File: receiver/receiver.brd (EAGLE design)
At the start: 100 x 80 mm, 3 parts, among them Q1 3.3

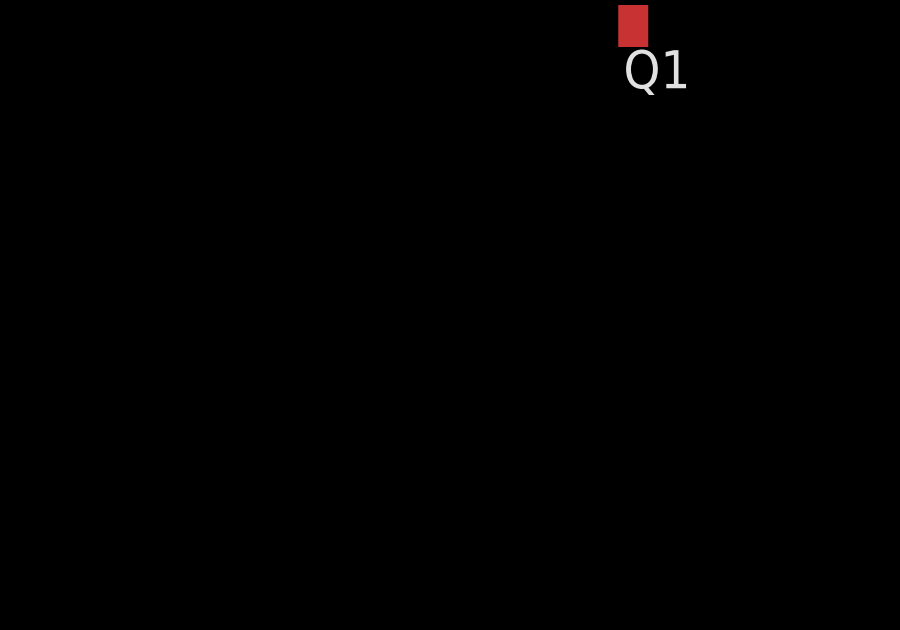
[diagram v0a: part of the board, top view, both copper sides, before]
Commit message: add yc164 resistor to receiver
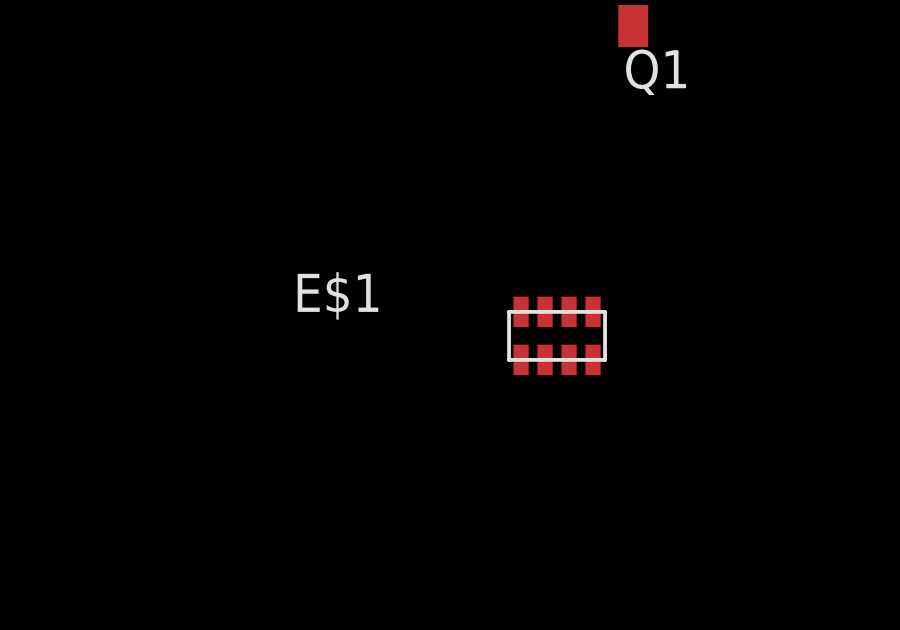
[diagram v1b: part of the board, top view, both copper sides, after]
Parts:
- added E$1: (no value), yc164:YC164
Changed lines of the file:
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@@
 <element name="U$1" library="cree_plcc4_rgb_led" package="4-PLCC" value="" x="45.72" y="25.4"/>
 <element name="Q1" library="adafruit" package="SOT23" value="3.3" x="49.53" y="53.34" rot="R180"/>
+<element name="E$1" library="yc164" package="YC164" value="" x="46.99" y="41.91"/>
 </elements>
 <signals>

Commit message: layout components
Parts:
- added U$2: CORE51822B, core51822b:CORE51822B
- added U$3: YC164, yc164:YC164
- E$1: value (none) -> YC164
- U$1: value (none) -> CREE_PLCC4_RGB_LED
- moved U$1 44.7 mm to (34.3, 68.6)
- moved E$1 25.4 mm to (31.8, 62.2)
- moved B1 23.9 mm to (38.1, 41.9)
- moved Q1 15.5 mm to (36.8, 62.2), turned to 0 degrees
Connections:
- removed net RAW: B1.24
- new net N$1: B1.24, Q1.3, U$1.P$2
- new net N$10: U$1.P$4, U$3.P$6
- new net N$11: U$1.P$1, U$3.P$5
- new net N$12: U$3.P$2, U$3.P$3
- new net N$14: U$1.P$3, U$3.P$8
- new net N$2: B1.22
- new net N$3: B1.20, U$3.P$4
- new net N$4: B1.19, U$3.P$1
- new net N$5: B1.5, U$3.P$7
- new net N$6: B1.6
- new net N$7: B1.1, E$1.P$7, E$1.P$8
- new net N$8: E$1.P$1, E$1.P$2, E$1.P$3, E$1.P$4, U$2.P25
- net GND: now also E$1.P$5, Q1.1, U$2.GND0, U$2.GND1
- net VCC: now also Q1.2, U$2.VCC
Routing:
- net GND: track 0.00 -> 78.5 mm, vias 0 -> 1
- net N$5: track 0.00 -> 56.8 mm, vias 0 -> 1
- net N$11: track 0.00 -> 43.5 mm
- net N$14: track 0.00 -> 34.3 mm, vias 0 -> 2
- net N$10: track 0.00 -> 33.5 mm
- net VCC: track 0.00 -> 20.9 mm
- net N$1: track 0.00 -> 15.3 mm, vias 0 -> 2
- net N$7: track 0.00 -> 0.81 mm
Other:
- board size 100 x 80 mm -> 47.9 x 59.7 mm

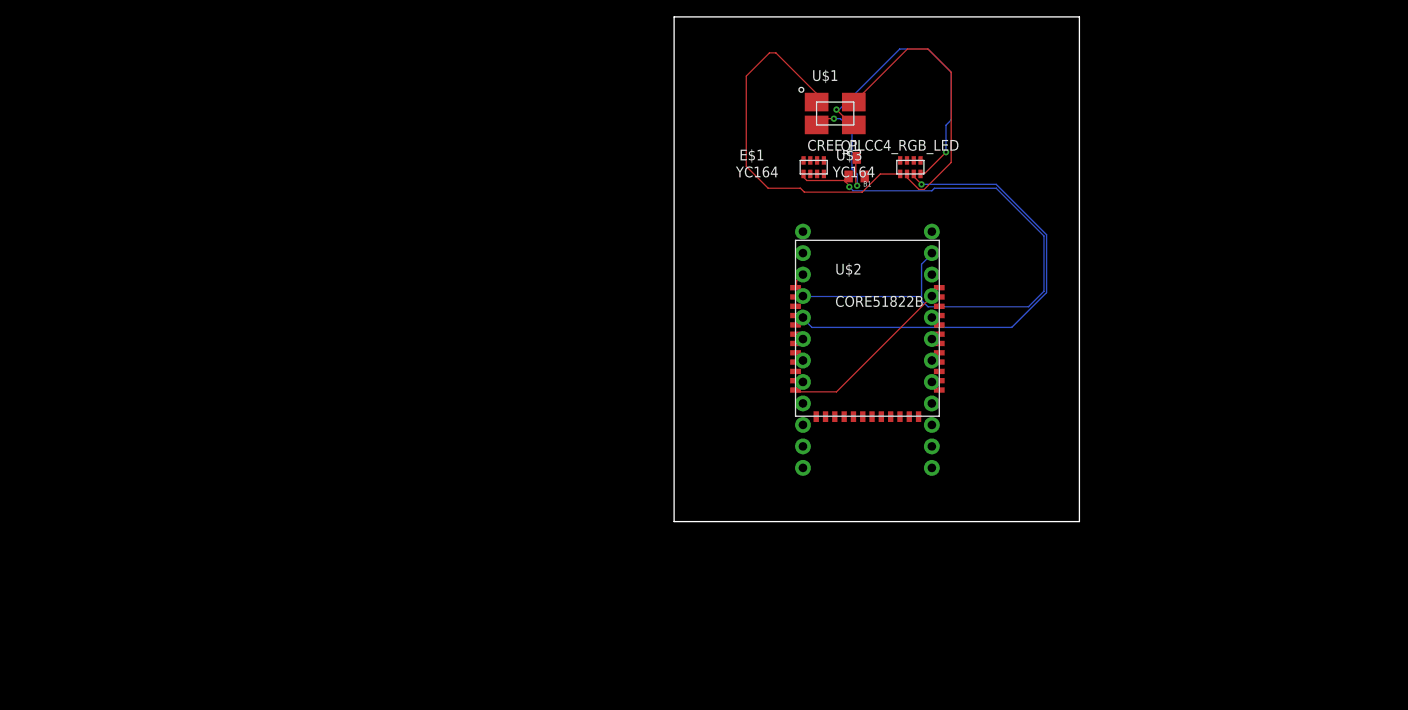
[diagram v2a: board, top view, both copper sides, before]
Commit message: add pts525-sm15 spst push button switch
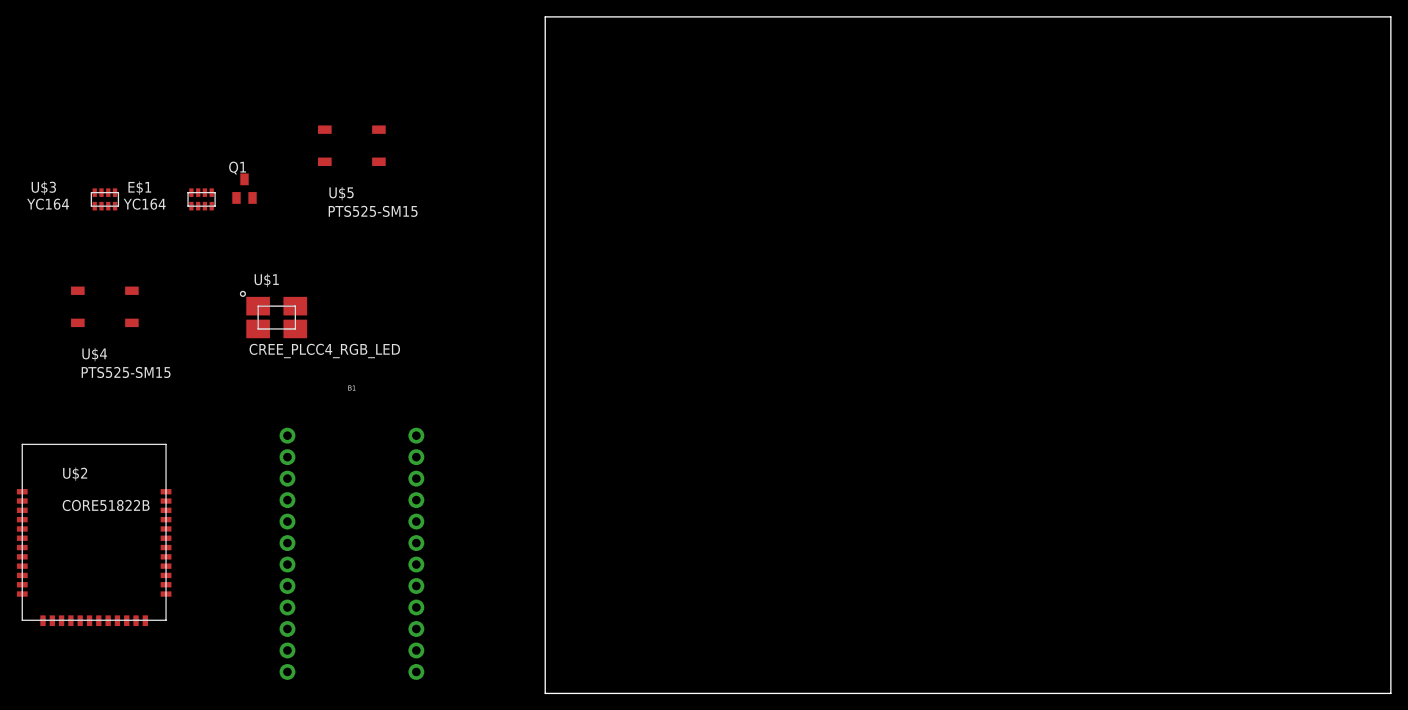
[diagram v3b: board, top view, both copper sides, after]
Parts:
- added U$4, U$5: PTS525-SM15, pts525-sm15:PTS525-SM15
- moved U$3 95.3 mm to (-52.1, 58.4)
- moved U$2 94.6 mm to (-53.3, 19.1)
- moved E$1 72.5 mm to (-40.6, 58.4)
- moved Q1 72.4 mm to (-35.6, 59.7)
- moved U$1 70.3 mm to (-31.8, 44.5)
- moved B1 65.6 mm to (-22.9, 17.8)
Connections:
- net N$1 renamed VIN
- net N$3 renamed LED-B
- net N$4 renamed LED-R
- net N$5 renamed LED-G
- net N$7 renamed TXO
- net N$8 renamed TXO-DIV
- removed net N$2: B1.22
- removed net N$6: B1.6
- new net PAIR: B1.6, U$4.P$3, U$4.P$4
- new net RESET: B1.22, U$5.P$3, U$5.P$4
- net GND: now also U$4.P$1, U$4.P$2, U$5.P$1, U$5.P$2
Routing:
- net GND: track 78.5 -> 0.00 mm, vias 1 -> 0
- net LED-G: track 56.8 -> 0.00 mm, vias 1 -> 0
- net N$11: track 43.5 -> 0.00 mm
- net N$14: track 34.3 -> 0.00 mm, vias 2 -> 0
- net N$10: track 33.5 -> 0.00 mm
- net VCC: track 20.9 -> 0.00 mm
- net VIN: track 15.3 -> 0.00 mm, vias 2 -> 0
- net TXO: track 0.81 -> 0.00 mm
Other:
- board size 47.9 x 59.7 mm -> 100 x 80 mm

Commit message: update board
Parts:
- removed B1: SPARKFUN_PRO_MICRO, SparkFun-Boards:SPARKFUN_PRO_MICRO
- added U$6, U$7: PROMICRO_HEADER, promicro_header:PROMICRO_HEADER
- moved U$2 134.7 mm to (78.7, 45.7)
- moved E$1 98.6 mm to (57.1, 45.7)
- moved Q1 94.0 mm to (55.9, 38.1)
- moved U$3 90.9 mm to (38.1, 47.0)
- moved U$4 86.2 mm to (31.8, 25.4)
- moved U$1 66.2 mm to (34.3, 39.4)
- moved U$5 52.2 mm to (11.4, 25.4)
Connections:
- new net ???: U$2.SWCLK
- new net ????: U$2.SWDIO
- new net ????????: U$6.P$4
- new net RXI: U$2.P24, U$7.P$2
- net GND: now also U$6.P$2, U$7.P$3, U$7.P$4; no longer B1.23, B1.3, B1.4
- net LED-B: now also U$6.P$5; no longer B1.20
- net LED-G: now also U$7.P$5; no longer B1.5
- net LED-R: now also U$6.P$6; no longer B1.19
- net PAIR: now also U$2.P29, U$7.P$6; no longer B1.6
- net RESET: now also U$6.P$3; no longer B1.22
- net TXO: now also U$7.P$1; no longer B1.1
- net VCC: no longer B1.21
- net VIN: now also U$6.P$1; no longer B1.24
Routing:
- net RESET: track 0.00 -> 67.5 mm
- net PAIR: track 0.00 -> 54.5 mm
- net VIN: track 0.00 -> 52.8 mm
- net VCC: track 0.00 -> 47.8 mm
- net LED-B: track 0.00 -> 18.1 mm
- net LED-R: track 0.00 -> 18.1 mm
- net TXO-DIV: track 0.00 -> 15.8 mm
- net N$14: track 0.00 -> 10.1 mm
- net N$11: track 0.00 -> 10.1 mm
- net N$10: track 0.00 -> 6.02 mm
- net N$12: track 0.00 -> 0.98 mm
- net TXO: track 0.00 -> 0.90 mm
- added copper zone on layer 1, net GND

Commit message: re-route
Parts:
- removed E$1, U$3: YC164, yc164:YC164
- removed Q1: 3.3, adafruit:SOT23
- removed U$1: CREE_PLCC4_RGB_LED, cree_plcc4_rgb_led:4-PLCC
- removed U$2: CORE51822B, core51822b:CORE51822B
- removed U$4, U$5: PTS525-SM15, pts525-sm15:PTS525-SM15
- removed U$6, U$7: PROMICRO_HEADER, promicro_header:PROMICRO_HEADER
- added B1, B2: PTS525-SM15, pts525-sm15:PTS525-SM15
- added D1: CREE_PLCC4_RGB_LED, cree_plcc4_rgb_led:4-PLCC
- added P1, P2: PROMICRO_HEADER, promicro_header:PROMICRO_HEADER
- added RA1, RA2: YC164, yc164:YC164
- added U1: CORE51822B, core51822b:CORE51822B
- added U2: 3.3, adafruit:SOT23
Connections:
- removed net ????????: U$6.P$4
- net ???: now also U1.SWCLK; no longer U$2.SWCLK
- net ????: now also U1.SWDIO; no longer U$2.SWDIO
- net GND: now also B1.P$1, B1.P$2, B2.P$1, B2.P$2, P1.P$3, P1.P$4, P2.P$2, RA2.P$5, U1.GND0, U1.GND1, U2.1; no longer E$1.P$5, Q1.1, U$2.GND0, U$2.GND1, U$4.P$1, U$4.P$2, U$5.P$1, U$5.P$2, U$6.P$2, U$7.P$3, U$7.P$4
- net LED-B: now also P2.P$5, RA1.P$4; no longer U$3.P$4, U$6.P$5
- net LED-G: now also P1.P$5, RA1.P$7; no longer U$3.P$7, U$7.P$5
- net LED-R: now also P2.P$6, RA1.P$1; no longer U$3.P$1, U$6.P$6
- net N$10: now also D1.P$4, RA1.P$6; no longer U$1.P$4, U$3.P$6
- net N$11: now also D1.P$1, RA1.P$5; no longer U$1.P$1, U$3.P$5
- net N$12: now also RA1.P$2, RA1.P$3; no longer U$3.P$2, U$3.P$3
- net N$14: now also D1.P$3, RA1.P$8; no longer U$1.P$3, U$3.P$8
- net PAIR: now also B1.P$3, B1.P$4, P1.P$6, U1.P29; no longer U$2.P29, U$4.P$3, U$4.P$4, U$7.P$6
- net RESET: now also B2.P$3, B2.P$4, P2.P$3; no longer U$5.P$3, U$5.P$4, U$6.P$3
- net RXI: now also P1.P$2, U1.P24; no longer U$2.P24, U$7.P$2
- net TXO: now also P1.P$1, RA2.P$7, RA2.P$8; no longer E$1.P$7, E$1.P$8, U$7.P$1
- net TXO-DIV: now also RA2.P$1, RA2.P$2, RA2.P$3, RA2.P$4, U1.P25; no longer E$1.P$1, E$1.P$2, E$1.P$3, E$1.P$4, U$2.P25
- net VCC: now also U1.VCC, U2.2; no longer Q1.2, U$2.VCC
- net VIN: now also D1.P$2, P2.P$1, U2.3; no longer Q1.3, U$1.P$2, U$6.P$1
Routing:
- net VCC: track 47.8 -> 9.23 mm
- net RESET: track 67.5 -> 31.1 mm
- net PAIR: track 54.5 -> 18.9 mm
- net RXI: track 0.00 -> 29.2 mm
- net VIN: track 52.8 -> 30.4 mm
- net LED-B: track 18.1 -> 6.63 mm
- net LED-R: track 18.1 -> 10.8 mm
- net N$11: track 10.1 -> 4.47 mm
- net N$14: track 10.1 -> 12.1 mm
- net N$10: track 6.02 -> 7.64 mm

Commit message: update board
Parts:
- U2: value 3.3 -> AZ1117IH; device adafruit:SOT23 -> az1117ih:AZ1117IH
- moved U2 3.06 mm to (56.1, 55.7)
- moved RA1 2.80 mm to (49.0, 57.8)
- moved RA2 2.80 mm to (49.0, 54.2)
- moved D1 1.30 mm to (44.3, 56.4)
- moved U1 1.02 mm to (72.1, 56.1)
- moved B1 0.13 mm to (55.9, 49.7)
- moved B2 0.13 mm to (47.1, 49.7), turned to 180 degrees
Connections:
- net GND: now also U2.ADJ/GND; no longer U2.1
- net VCC: now also U2.OUTPUT, U2.VOUT; no longer U2.2
- net VIN: now also U2.INPUT; no longer U2.3
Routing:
- net PAIR: track 18.9 -> 70.0 mm
- net VIN: track 30.4 -> 55.4 mm
- net RESET: track 31.1 -> 52.1 mm
- net TXO-DIV: track 15.4 -> 33.1 mm
- net LED-B: track 6.63 -> 15.6 mm
- net TXO: track 0.92 -> 9.30 mm
- net VCC: track 9.23 -> 16.8 mm
- net LED-R: track 10.8 -> 18.2 mm
- net N$14: track 12.1 -> 8.75 mm
- net N$10: track 7.64 -> 5.83 mm
- net RXI: track 29.2 -> 30.1 mm
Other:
- board text added: "Jesse Martin"
- board text added: "Kbd Receiver Version 1"

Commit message: include programming header on board
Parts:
- added U$1: PROG_HEADER, prog_header:PROG_HEADER
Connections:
- removed net ???: U1.SWCLK
- removed net ????: U1.SWDIO
- new net SWCLK: U$1.SWCLK, U1.SWCLK
- new net SWDIO: U$1.SWDIO, U1.SWDIO
- net GND: now also U$1.GND
- net VCC: now also U$1.VCC
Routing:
- net VCC: track 16.8 -> 54.8 mm
- net SWCLK: track 0.00 -> 4.75 mm
- net SWDIO: track 0.00 -> 3.33 mm
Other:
- board size 100 x 80 mm -> 49.2 x 26.7 mm
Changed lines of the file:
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@@
 <setting verticaltext="up"/>
 </settings>
-<grid distance="15.25" unitdist="mm" unit="mm" style="lines" multiple="1" display="yes" altdistance="5" altunitdist="mil" altunit="mil"/>
+<grid distance="2.54" unitdist="mm" unit="mm" style="lines" multiple="1" display="yes" altdistance="5" altunitdist="mil" altunit="mil"/>
 <layers>
 <layer number="1" name="Top" color="4" fill="1" visible="yes" active="yes"/>
@@
 <board>
 <plain>
-<wire x1="0" y1="0" x2="100" y2="0" width="0" layer="20"/>
-<wire x1="100" y1="0" x2="100" y2="80" width="0" layer="20"/>
-<wire x1="100" y1="80" x2="0" y2="80" width="0" layer="20"/>
-<wire x1="0" y1="80" x2="0" y2="0" width="0" layer="20"/>
+<wire x1="38.1" y1="40.64" x2="87.3" y2="40.64" width="0" layer="20"/>
+<wire x1="87.3" y1="40.64" x2="87.3" y2="67.3" width="0" layer="20"/>
+<wire x1="87.3" y1="67.3" x2="38.1" y2="67.3" width="0" layer="20"/>
+<wire x1="38.1" y1="67.3" x2="38.1" y2="40.64" width="0" layer="20"/>
 <text x="65.074" y="63.667" size="1.778" layer="25" font="vector">Jesse Martin</text>
 <text x="67.487" y="54.777" size="1.27" layer="25" font="vector">Kbd Receiver
@@
 <element name="P1" library="promicro_header" package="PROMICRO_HEADER" value="PROMICRO_HEADER" x="52.07" y="45.75" smashed="yes" rot="R90"/>
 <element name="U2" library="az1117ih" package="AZ1117IH" value="AZ1117IH" x="56.144" y="55.743" rot="R90"/>
+<element name="U$1" library="prog_header" package="PROG_HEADER" value="PROG_HEADER" x="83.185" y="52.197" rot="R180"/>
 </elements>
 <signals>
@@
 <contactref element="P1" pad="P$3"/>
 <contactref element="P1" pad="P$4"/>
-<polygon width="0.1524" layer="1">
-<vertex x="3.81" y="68.58"/>
-<vertex x="3.81" y="8.89"/>
-<vertex x="91.44" y="8.89"/>
-<vertex x="92.71" y="10.16"/>
-<vertex x="92.71" y="66.04"/>
-<vertex x="88.9" y="69.85"/>
-<vertex x="5.08" y="69.85"/>
-</polygon>
 <wire x1="69.2912" y1="50.8508" x2="69.297303125" y2="50.96495" width="0.3048" layer="1"/>
 <contactref element="U2" pad="ADJ/GND"/>
+<contactref element="U$1" pad="GND"/>
+<polygon width="0.1524" layer="1">
+<vertex x="40.64" y="66.04"/>
+<vertex x="86.36" y="66.04"/>
+<vertex x="86.36" y="43.18"/>
+<vertex x="40.64" y="43.18"/>
+</polygon>
 <wire x1="63.636" y1="49.934" x2="69.2912" y2="50.8508" width="0" layer="19" extent="1-1"/>
 <wire x1="50.317" y1="47.757" x2="52.68" y2="51.557" width="0" layer="19" extent="1-1"/>
@@
 <wire x1="53.086" y1="55.88" x2="53.044" y2="55.743" width="0.3048" layer="1"/>
 <wire x1="59.2328" y1="55.88" x2="59.244" y2="55.743" width="0.3048" layer="1"/>
+<contactref element="U$1" pad="VCC"/>
+<wire x1="82.9818" y1="49.4538" x2="82.9818" y2="51.9684" width="0.3048" layer="1"/>
+<wire x1="81.5848" y1="48.0568" x2="82.9818" y2="49.4538" width="0.3048" layer="1"/>
+<wire x1="79.629" y1="48.0568" x2="81.5848" y2="48.0568" width="0.3048" layer="1"/>
+<wire x1="64.8208" y1="62.865" x2="79.629" y2="48.0568" width="0.3048" layer="1"/>
+<wire x1="62.5856" y1="62.865" x2="64.8208" y2="62.865" width="0.3048" layer="1"/>
+<wire x1="61.1886" y1="61.468" x2="62.5856" y2="62.865" width="0.3048" layer="1"/>
+<wire x1="61.1886" y1="55.3212" x2="61.1886" y2="61.468" width="0.3048" layer="1"/>
+<wire x1="82.9818" y1="51.9684" x2="83.185" y2="52.197" width="0.3048" layer="1"/>
 </signal>
 <signal name="LED-G">
@@
 <wire x1="48.3362" y1="45.5422" x2="48.26" y2="45.75" width="0.3048" layer="1"/>
 </signal>
-<signal name="???">
+<signal name="SWCLK">
 <contactref element="U1" pad="SWCLK"/>
-</signal>
-<signal name="????">
+<contactref element="U$1" pad="SWCLK"/>
+<wire x1="81.3054" y1="56.7182" x2="80.7466" y2="56.7182" width="0.3048" layer="1"/>
+<wire x1="81.8642" y1="57.277" x2="81.3054" y2="56.7182" width="0.3048" layer="1"/>
+<wire x1="81.8642" y1="58.674" x2="81.8642" y2="57.277" width="0.3048" layer="1"/>
+<wire x1="82.9818" y1="59.7916" x2="81.8642" y2="58.674" width="0.3048" layer="1"/>
+<wire x1="80.7466" y1="56.7182" x2="80.636" y2="56.534" width="0.3048" layer="1"/>
+<wire x1="82.9818" y1="59.7916" x2="83.185" y2="59.817" width="0.3048" layer="1"/>
+</signal>
+<signal name="SWDIO">
+<contactref element="U$1" pad="SWDIO"/>
 <contactref element="U1" pad="SWDIO"/>
+<wire x1="81.3054" y1="55.6006" x2="80.7466" y2="55.6006" width="0.3048" layer="1"/>
+<wire x1="82.9818" y1="57.277" x2="81.3054" y2="55.6006" width="0.3048" layer="1"/>
+<wire x1="80.7466" y1="55.6006" x2="80.636" y2="55.434" width="0.3048" layer="1"/>
+<wire x1="82.9818" y1="57.277" x2="83.185" y2="57.277" width="0.3048" layer="1"/>
 </signal>
 </signals>
